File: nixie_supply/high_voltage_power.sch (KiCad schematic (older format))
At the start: 14 parts

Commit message: minor cleanups
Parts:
- C3: renamed from C?; value C_HV -> 10uF 315V
- D1: renamed from D?; value D_HV -> D_HV 400V
- gave numbers to parts that had none: 12
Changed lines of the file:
@@
 $EndDescr
 $Comp
-L 4047 U?
+L 4047 U2
 U 1 1 590CECA6
 P 4200 3000
-F 0 "U?" H 4200 2950 60  0000 C CNN
+F 0 "U2" H 4200 2950 60  0000 C CNN
 F 1 "4047" H 4200 2850 60  0000 C CNN
 F 2 "" H 4200 2950 60  0001 C CNN
@@
 $EndComp
 $Comp
-L GND #PWR?
+L GND #PWR03
 U 1 1 590CED04
 P 3200 3750
-F 0 "#PWR?" H 3200 3500 50  0001 C CNN
+F 0 "#PWR03" H 3200 3500 50  0001 C CNN
 F 1 "GND" H 3200 3600 50  0000 C CNN
 F 2 "" H 3200 3750 50  0000 C CNN
@@
 $EndComp
 $Comp
-L C C?
+L C C1
 U 1 1 590CF22D
 P 2950 2800
-F 0 "C?" H 2975 2900 50  0000 L CNN
+F 0 "C1" H 2975 2900 50  0000 L CNN
 F 1 "0.001uF" H 2650 2700 50  0000 L CNN
 F 2 "" H 2988 2650 50  0000 C CNN
@@
 $EndComp
 $Comp
-L R R?
+L R R4
 U 1 1 590CF24E
 P 3200 2800
-F 0 "R?" V 3280 2800 50  0000 C CNN
+F 0 "R4" V 3280 2800 50  0000 C CNN
 F 1 "10K" V 3200 2800 50  0000 C CNN
 F 2 "" V 3130 2800 50  0000 C CNN
@@
 $EndComp
 $Comp
-L GND #PWR?
+L GND #PWR04
 U 1 1 590CF44C
 P 5100 3400
-F 0 "#PWR?" H 5100 3150 50  0001 C CNN
+F 0 "#PWR04" H 5100 3150 50  0001 C CNN
 F 1 "GND" H 5100 3250 50  0000 C CNN
 F 2 "" H 5100 3400 50  0000 C CNN
@@
 NoConn ~ 4900 3050
 $Comp
-L R R?
+L R R6
 U 1 1 590CF674
 P 5400 3150
-F 0 "R?" V 5480 3150 50  0000 C CNN
+F 0 "R6" V 5480 3150 50  0000 C CNN
 F 1 "120" V 5400 3150 50  0000 C CNN
 F 2 "" V 5330 3150 50  0000 C CNN
@@
 	4900 3150 5250 3150
 $Comp
-L FQPF4N90CT Q?
+L FQPF4N90CT Q1
 U 1 1 590CFA7D
 P 5950 3100
-F 0 "Q?" H 6150 3175 50  0000 L CNN
+F 0 "Q1" H 6150 3175 50  0000 L CNN
 F 1 "FQPF4N90CT" H 6150 3100 50  0000 L CNN
 F 2 "TO_220" H 6150 3025 50  0001 L CIN
@@
 	5550 3150 5750 3150
 $Comp
-L L L?
+L L L1
 U 1 1 590CFB8C
 P 6050 2650
-F 0 "L?" V 6000 2650 50  0000 C CNN
+F 0 "L1" V 6000 2650 50  0000 C CNN
 F 1 "100uH" V 6125 2650 50  0000 C CNN
 F 2 "" H 6050 2650 50  0000 C CNN
@@
 	6050 2450 6050 2500
 $Comp
-L GND #PWR?
+L GND #PWR05
 U 1 1 590CFDA8
 P 6050 3400
-F 0 "#PWR?" H 6050 3150 50  0001 C CNN
+F 0 "#PWR05" H 6050 3150 50  0001 C CNN
 F 1 "GND" H 6050 3250 50  0000 C CNN
 F 2 "" H 6050 3400 50  0000 C CNN
@@
 	6050 3300 6050 3400
 $Comp
-L D_HV D?
+L D_HV D1
 U 1 1 590CFF0A
 P 6500 2850
-F 0 "D?" H 6500 2950 50  0000 C CNN
-F 1 "D_HV" H 6500 2750 50  0000 C CNN
+F 0 "D1" H 6500 2950 50  0000 C CNN
+F 1 "D_HV 400V" H 6500 2750 50  0000 C CNN
 F 2 "" H 6500 2850 50  0000 C CNN
 F 3 "" H 6500 2850 50  0000 C CNN
@@
 Connection ~ 6050 2850
 $Comp
-L C_HV C?
+L C_HV C3
 U 1 1 590D050D
 P 6950 3100
-F 0 "C?" H 6975 3200 50  0000 L CNN
-F 1 "C_HV" H 6975 3000 50  0000 L CNN
+F 0 "C3" H 6975 3200 50  0000 L CNN
+F 1 "10uF 315V" H 6975 3000 50  0000 L CNN
 F 2 "" H 6988 2950 50  0000 C CNN
 F 3 "" H 6950 3100 50  0000 C CNN
@@
 $EndComp
 Wire Wire Line
-	6650 2850 6950 2850
+	6650 2850 7200 2850
 Wire Wire Line
 	6950 2650 6950 2950
 $Comp
-L GND #PWR?
+L GND #PWR06
 U 1 1 590D056B
 P 6950 3400
-F 0 "#PWR?" H 6950 3150 50  0001 C CNN
+F 0 "#PWR06" H 6950 3150 50  0001 C CNN
 F 1 "GND" H 6950 3250 50  0000 C CNN
 F 2 "" H 6950 3400 50  0000 C CNN
@@
 Connection ~ 6950 2850
 $Comp
-L LM741 U?
+L LM741 U1
 U 1 1 590D1633
 P 3700 4700
-F 0 "U?" H 3700 4950 50  0000 L CNN
+F 0 "U1" H 3700 4950 50  0000 L CNN
 F 1 "LM741" H 3700 4850 50  0000 L CNN
 F 2 "" H 3750 4750 50  0000 C CNN
@@
 	4900 4700 4900 3250
 $Comp
-L GND #PWR?
+L GND #PWR07
 U 1 1 590D19B4
 P 3600 5100
-F 0 "#PWR?" H 3600 4850 50  0001 C CNN
+F 0 "#PWR07" H 3600 4850 50  0001 C CNN
 F 1 "GND" H 3600 4950 50  0000 C CNN
 F 2 "" H 3600 5100 50  0000 C CNN
@@
 	3600 5000 3600 5100
 $Comp
-L +5V #PWR?
+L +5V #PWR08
 U 1 1 590D1D3C
 P 2600 4800
-F 0 "#PWR?" H 2600 4650 50  0001 C CNN
+F 0 "#PWR08" H 2600 4650 50  0001 C CNN
 F 1 "+5V" H 2600 4940 50  0000 C CNN
 F 2 "" H 2600 4800 50  0000 C CNN
@@
 $EndComp
 $Comp
-L R R?
+L R R1
 U 1 1 590D1D88
 P 2850 4600
-F 0 "R?" V 2930 4600 50  0000 C CNN
+F 0 "R1" V 2930 4600 50  0000 C CNN
 F 1 "220K" V 2850 4600 50  0000 C CNN
 F 2 "" V 2780 4600 50  0000 C CNN
@@
 $EndComp
 $Comp
-L R R?
+L R R3
 U 1 1 590D1DB1
 P 3050 5150
-F 0 "R?" V 3130 5150 50  0000 C CNN
+F 0 "R3" V 3130 5150 50  0000 C CNN
 F 1 "4.7K" V 3050 5150 50  0000 C CNN
 F 2 "" V 2980 5150 50  0000 C CNN
@@
 $EndComp
 $Comp
-L R R?
+L R R2
 U 1 1 590D1DDC
 P 2850 4800
-F 0 "R?" V 2930 4800 50  0000 C CNN
+F 0 "R2" V 2930 4800 50  0000 C CNN
 F 1 "1.2K" V 2850 4800 50  0000 C CNN
 F 2 "" V 2780 4800 50  0000 C CNN
@@
 $EndComp
 $Comp
-L R R?
+L R R5
 U 1 1 590D1E09
 P 3250 5150
-F 0 "R?" V 3330 5150 50  0000 C CNN
+F 0 "R5" V 3330 5150 50  0000 C CNN
 F 1 "4.7K" V 3250 5150 50  0000 C CNN
 F 2 "" V 3180 5150 50  0000 C CNN
@@
 Connection ~ 3250 4800
 $Comp
-L GND #PWR?
+L GND #PWR09
 U 1 1 590D2323
 P 3150 5400
-F 0 "#PWR?" H 3150 5150 50  0001 C CNN
+F 0 "#PWR09" H 3150 5150 50  0001 C CNN
 F 1 "GND" H 3150 5250 50  0000 C CNN
 F 2 "" H 3150 5400 50  0000 C CNN
@@
 220V
 $Comp
-L +5V #PWR?
+L +5V #PWR010
 U 1 1 590D45F5
 P 6050 3900
-F 0 "#PWR?" H 6050 3750 50  0001 C CNN
+F 0 "#PWR010" H 6050 3750 50  0001 C CNN
 F 1 "+5V" H 6050 4040 50  0000 C CNN
 F 2 "" H 6050 3900 50  0000 C CNN
@@
 GND
 $Comp
-L GND #PWR?
+L GND #PWR011
 U 1 1 590D826E
 P 6200 4550
-F 0 "#PWR?" H 6200 4300 50  0001 C CNN
+F 0 "#PWR011" H 6200 4300 50  0001 C CNN
 F 1 "GND" H 6200 4400 50  0000 C CNN
 F 2 "" H 6200 4550 50  0000 C CNN
@@
 	6000 4550 6200 4550
 $Comp
-L +12V #PWR?
+L +12V #PWR012
 U 1 1 5910BACF
 P 3200 3300
-F 0 "#PWR?" H 3200 3150 50  0001 C CNN
+F 0 "#PWR012" H 3200 3150 50  0001 C CNN
 F 1 "+12V" H 3200 3440 50  0000 C CNN
 F 2 "" H 3200 3300 50  0000 C CNN
@@
 $EndComp
 $Comp
-L +12V #PWR?
+L +12V #PWR013
 U 1 1 5910BAFD
 P 5300 2550
-F 0 "#PWR?" H 5300 2400 50  0001 C CNN
+F 0 "#PWR013" H 5300 2400 50  0001 C CNN
 F 1 "+12V" H 5300 2690 50  0000 C CNN
 F 2 "" H 5300 2550 50  0000 C CNN
@@
 $EndComp
 $Comp
-L +12V #PWR?
+L +12V #PWR014
 U 1 1 5910BB2B
 P 6050 2450
-F 0 "#PWR?" H 6050 2300 50  0001 C CNN
+F 0 "#PWR014" H 6050 2300 50  0001 C CNN
 F 1 "+12V" H 6050 2590 50  0000 C CNN
 F 2 "" H 6050 2450 50  0000 C CNN
@@
 $EndComp
 $Comp
-L +12V #PWR?
+L +12V #PWR015
 U 1 1 5910BB59
 P 6200 4350
-F 0 "#PWR?" H 6200 4200 50  0001 C CNN
+F 0 "#PWR015" H 6200 4200 50  0001 C CNN
 F 1 "+12V" H 6200 4490 50  0000 C CNN
 F 2 "" H 6200 4350 50  0000 C CNN
@@
 12V
 $Comp
-L +5V #PWR?
+L +5V #PWR016
 U 1 1 5910BD01
 P 3600 4300
-F 0 "#PWR?" H 3600 4150 50  0001 C CNN
+F 0 "#PWR016" H 3600 4150 50  0001 C CNN
 F 1 "+5V" H 3600 4440 50  0000 C CNN
 F 2 "" H 3600 4300 50  0000 C CNN
@@
 $EndComp
 $Comp
-L C C?
+L C C2
 U 1 1 5910C445
 P 3200 3550
-F 0 "C?" H 3225 3650 50  0000 L CNN
+F 0 "C2" H 3225 3650 50  0000 L CNN
 F 1 "0.1uF" H 3225 3450 50  0000 L CNN
 F 2 "" H 3238 3400 50  0000 C CNN
@@
 	3450 3750 3200 3750
 $Comp
-L +220V #PWR?
+L +220V #PWR017
 U 1 1 5910CAB3
 P 2600 4600
-F 0 "#PWR?" H 2600 4450 50  0001 C CNN
+F 0 "#PWR017" H 2600 4450 50  0001 C CNN
 F 1 "+220V" H 2600 4740 50  0000 C CNN
 F 2 "" H 2600 4600 50  0000 C CNN
@@
 $EndComp
 $Comp
-L +220V #PWR?
+L +220V #PWR018
 U 1 1 5910CAE3
 P 6950 2650
-F 0 "#PWR?" H 6950 2500 50  0001 C CNN
+F 0 "#PWR018" H 6950 2500 50  0001 C CNN
 F 1 "+220V" H 6950 2790 50  0000 C CNN
 F 2 "" H 6950 2650 50  0000 C CNN
@@
 $EndComp
 $Comp
-L +220V #PWR?
+L +220V #PWR019
 U 1 1 5910CB13
 P 6550 3900
-F 0 "#PWR?" H 6550 3750 50  0001 C CNN
+F 0 "#PWR019" H 6550 3750 50  0001 C CNN
 F 1 "+220V" H 6550 4040 50  0000 C CNN
 F 2 "" H 6550 3900 50  0000 C CNN
@@
 	1    0    0    -1
 $EndComp
+$Comp
+L PWR_FLAG #FLG020
+U 1 1 591378F6
+P 7200 2850
+F 0 "#FLG020" H 7200 2945 50  0001 C CNN
+F 1 "PWR_FLAG" H 7200 3030 50  0000 C CNN
+F 2 "" H 7200 2850 50  0000 C CNN
+F 3 "" H 7200 2850 50  0000 C CNN
+	1    7200 2850
+	1    0    0    -1
+$EndComp

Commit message: Footprint associations
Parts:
- C1: footprint (none) -> Capacitors_THT:C_Disc_D5.0mm_W2.5mm_P5.00mm
- C2: footprint (none) -> Capacitors_THT:C_Axial_L5.1mm_D3.1mm_P7.50mm_Horizontal
- C3: footprint (none) -> Capacitors_THT:CP_Radial_D10.0mm_P3.80mm
- D1: footprint (none) -> Diodes_THT:D_T-1_P5.08mm_Horizontal
- L1: footprint (none) -> Inductors_NEOSID:Neosid_Inductor_Sd8
- Q1: footprint TO_220 -> TO_SOT_Packages_THT:TO-220_Vertical
- R1, R3: footprint (none) -> hv:R_Axial_DIN0309_L9.0mm_D3.2mm_P12.70mm_Horizontal_Thick
- R2, R4, R5, R6: footprint (none) -> Resistors_THT:R_Axial_DIN0207_L6.3mm_D2.5mm_P10.16mm_Horizontal
- U1: footprint (none) -> Housings_DIP:DIP-8_W7.62mm
- U2: footprint (none) -> Housings_DIP:DIP-14_W7.62mm
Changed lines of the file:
@@
 F 0 "U2" H 4200 2950 60  0000 C CNN
 F 1 "4047" H 4200 2850 60  0000 C CNN
-F 2 "" H 4200 2950 60  0001 C CNN
+F 2 "Housings_DIP:DIP-14_W7.62mm" H 4200 2950 60  0001 C CNN
 F 3 "" H 4200 2950 60  0001 C CNN
 	1    4200 3000
@@
 F 0 "C1" H 2975 2900 50  0000 L CNN
 F 1 "0.001uF" H 2650 2700 50  0000 L CNN
-F 2 "" H 2988 2650 50  0000 C CNN
+F 2 "Capacitors_THT:C_Disc_D5.0mm_W2.5mm_P5.00mm" H 2988 2650 50  0001 C CNN
 F 3 "" H 2950 2800 50  0000 C CNN
 	1    2950 2800
@@
 F 0 "R4" V 3280 2800 50  0000 C CNN
 F 1 "10K" V 3200 2800 50  0000 C CNN
-F 2 "" V 3130 2800 50  0000 C CNN
+F 2 "Resistors_THT:R_Axial_DIN0207_L6.3mm_D2.5mm_P10.16mm_Horizontal" V 3130 2800 50  0001 C CNN
 F 3 "" H 3200 2800 50  0000 C CNN
 	1    3200 2800
@@
 F 0 "R6" V 5480 3150 50  0000 C CNN
 F 1 "120" V 5400 3150 50  0000 C CNN
-F 2 "" V 5330 3150 50  0000 C CNN
+F 2 "Resistors_THT:R_Axial_DIN0207_L6.3mm_D2.5mm_P10.16mm_Horizontal" V 5330 3150 50  0001 C CNN
 F 3 "" H 5400 3150 50  0000 C CNN
 	1    5400 3150
@@
 U 1 1 590CFA7D
 P 5950 3100
+AR Path="/590CFA7D" Ref="Q1"  Part="1"
+AR Path="/5910AEC0/590CFA7D" Ref="Q1"  Part="1"
 F 0 "Q1" H 6150 3175 50  0000 L CNN
 F 1 "FQPF4N90CT" H 6150 3100 50  0000 L CNN
-F 2 "TO_220" H 6150 3025 50  0001 L CIN
+F 2 "TO_SOT_Packages_THT:TO-220_Vertical" H 6150 3025 50  0001 L CIN
 F 3 "" H 5950 3100 50  0000 L CNN
 	1    5950 3100
 	1    0    0    -1
 $EndComp
-Wire Wire Line
-	5550 3150 5750 3150
 $Comp
 L L L1
@@
 F 0 "L1" V 6000 2650 50  0000 C CNN
 F 1 "100uH" V 6125 2650 50  0000 C CNN
-F 2 "" H 6050 2650 50  0000 C CNN
+F 2 "Inductors_NEOSID:Neosid_Inductor_Sd8" H 6050 2650 50  0001 C CNN
 F 3 "" H 6050 2650 50  0000 C CNN
 	1    6050 2650
 	1    0    0    -1
 $EndComp
-Wire Wire Line
-	6050 2800 6050 2900
 Wire Wire Line
 	6050 2450 6050 2500
@@
 	1    0    0    -1
 $EndComp
-Wire Wire Line
-	6050 3300 6050 3400
 $Comp
 L D_HV D1
@@
 F 0 "D1" H 6500 2950 50  0000 C CNN
 F 1 "D_HV 400V" H 6500 2750 50  0000 C CNN
-F 2 "" H 6500 2850 50  0000 C CNN
+F 2 "Diodes_THT:D_T-1_P5.08mm_Horizontal" H 6500 2850 50  0001 C CNN
 F 3 "" H 6500 2850 50  0000 C CNN
 	1    6500 2850
@@
 F 0 "C3" H 6975 3200 50  0000 L CNN
 F 1 "10uF 315V" H 6975 3000 50  0000 L CNN
-F 2 "" H 6988 2950 50  0000 C CNN
+F 2 "Capacitors_THT:CP_Radial_D10.0mm_P3.80mm" H 6988 2950 50  0001 C CNN
 F 3 "" H 6950 3100 50  0000 C CNN
 	1    6950 3100
@@
 F 0 "U1" H 3700 4950 50  0000 L CNN
 F 1 "LM741" H 3700 4850 50  0000 L CNN
-F 2 "" H 3750 4750 50  0000 C CNN
+F 2 "Housings_DIP:DIP-8_W7.62mm" H 3750 4750 50  0001 C CNN
 F 3 "" H 3850 4850 50  0000 C CNN
 	1    3700 4700
@@
 F 0 "R1" V 2930 4600 50  0000 C CNN
 F 1 "220K" V 2850 4600 50  0000 C CNN
-F 2 "" V 2780 4600 50  0000 C CNN
+F 2 "hv:R_Axial_DIN0309_L9.0mm_D3.2mm_P12.70mm_Horizontal_Thick" V 2780 4600 50  0001 C CNN
 F 3 "" H 2850 4600 50  0000 C CNN
 	1    2850 4600
@@
 F 0 "R3" V 3130 5150 50  0000 C CNN
 F 1 "4.7K" V 3050 5150 50  0000 C CNN
-F 2 "" V 2980 5150 50  0000 C CNN
+F 2 "hv:R_Axial_DIN0309_L9.0mm_D3.2mm_P12.70mm_Horizontal_Thick" V 2980 5150 50  0001 C CNN
 F 3 "" H 3050 5150 50  0000 C CNN
 	1    3050 5150
@@
 F 0 "R2" V 2930 4800 50  0000 C CNN
 F 1 "1.2K" V 2850 4800 50  0000 C CNN
-F 2 "" V 2780 4800 50  0000 C CNN
+F 2 "Resistors_THT:R_Axial_DIN0207_L6.3mm_D2.5mm_P10.16mm_Horizontal" V 2780 4800 50  0001 C CNN
 F 3 "" H 2850 4800 50  0000 C CNN
 	1    2850 4800
@@
 F 0 "R5" V 3330 5150 50  0000 C CNN
 F 1 "4.7K" V 3250 5150 50  0000 C CNN
-F 2 "" V 3180 5150 50  0000 C CNN
+F 2 "Resistors_THT:R_Axial_DIN0207_L6.3mm_D2.5mm_P10.16mm_Horizontal" V 3180 5150 50  0001 C CNN
 F 3 "" H 3250 5150 50  0000 C CNN
 	1    3250 5150
@@
 F 0 "C2" H 3225 3650 50  0000 L CNN
 F 1 "0.1uF" H 3225 3450 50  0000 L CNN
-F 2 "" H 3238 3400 50  0000 C CNN
+F 2 "Capacitors_THT:C_Axial_L5.1mm_D3.1mm_P7.50mm_Horizontal" H 3238 3400 50  0001 C CNN
 F 3 "" H 3200 3550 50  0000 C CNN
 	1    3200 3550
@@
 	1    0    0    -1
 $EndComp
+Wire Wire Line
+	6050 2800 6050 2900
+Wire Wire Line
+	6050 3300 6050 3400
+Wire Wire Line
+	5550 3150 5750 3150
 $EndSCHEMATC

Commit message: Clock board layout
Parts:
- U1: symbol LM741 -> LM741-RESCUE-nixie_supply
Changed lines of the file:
@@
 EESchema Schematic File Version 2
+LIBS:nixie_supply-rescue
 LIBS:power
 LIBS:device
@@
 Connection ~ 6950 2850
 $Comp
-L LM741 U1
+L LM741-RESCUE-nixie_supply U1
 U 1 1 590D1633
 P 3700 4700

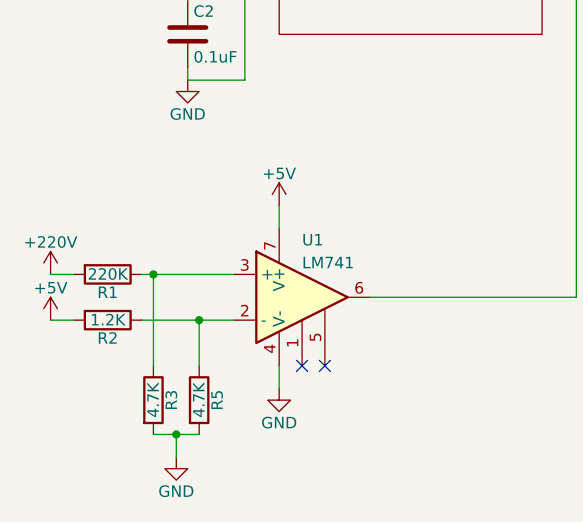
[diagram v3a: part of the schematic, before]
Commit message: Supply board mk2: reduced time base noise, upped some clearances, added ground plane
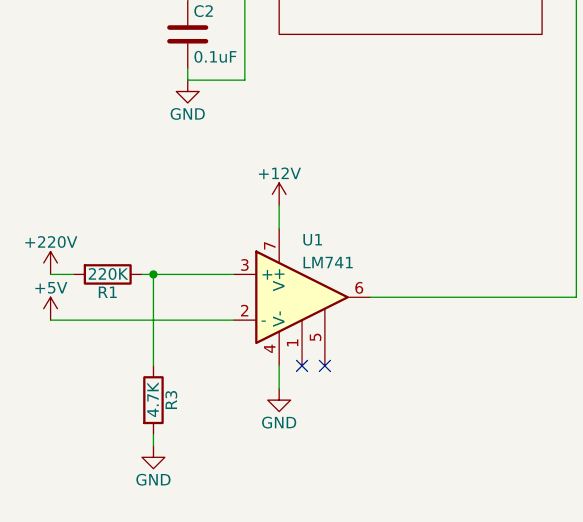
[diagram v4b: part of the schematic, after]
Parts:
- removed R2: 1.2K, Resistors_THT:R_Axial_DIN0207_L6.3mm_D2.5mm_P10.16mm_Horizontal, symbol R
- removed R5: 4.7K, Resistors_THT:R_Axial_DIN0207_L6.3mm_D2.5mm_P10.16mm_Horizontal, symbol R
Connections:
- net +12V: now also U1.7 (V+)
- net +5V: now also U1.2 (-); no longer U1.7 (V+)
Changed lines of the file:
@@
 $EndComp
-Wire Wire Line
-	3600 4300 3600 4400
 Wire Wire Line
 	3600 5000 3600 5100
@@
 	1    0    0    -1
 $EndComp
-$Comp
-L R R2
-U 1 1 590D1DDC
-P 2850 4800
-F 0 "R2" V 2930 4800 50  0000 C CNN
-F 1 "1.2K" V 2850 4800 50  0000 C CNN
-F 2 "Resistors_THT:R_Axial_DIN0207_L6.3mm_D2.5mm_P10.16mm_Horizontal" V 2780 4800 50  0001 C CNN
-F 3 "" H 2850 4800 50  0000 C CNN
-	1    2850 4800
-	0    1    1    0
-$EndComp
-$Comp
-L R R5
-U 1 1 590D1E09
-P 3250 5150
-F 0 "R5" V 3330 5150 50  0000 C CNN
-F 1 "4.7K" V 3250 5150 50  0000 C CNN
-F 2 "Resistors_THT:R_Axial_DIN0207_L6.3mm_D2.5mm_P10.16mm_Horizontal" V 3180 5150 50  0001 C CNN
-F 3 "" H 3250 5150 50  0000 C CNN
-	1    3250 5150
-	1    0    0    -1
-$EndComp
 Wire Wire Line
 	2600 4600 2700 4600
 Wire Wire Line
 	3000 4600 3400 4600
-Wire Wire Line
-	3400 4800 3000 4800
-Wire Wire Line
-	2600 4800 2700 4800
 Wire Wire Line
 	3050 5000 3050 4600
 Connection ~ 3050 4600
-Wire Wire Line
-	3250 5000 3250 4800
-Connection ~ 3250 4800
 $Comp
 L GND #PWR09
 U 1 1 590D2323
-P 3150 5400
-F 0 "#PWR09" H 3150 5150 50  0001 C CNN
-F 1 "GND" H 3150 5250 50  0000 C CNN
-F 2 "" H 3150 5400 50  0000 C CNN
-F 3 "" H 3150 5400 50  0000 C CNN
-	1    3150 5400
-	1    0    0    -1
-$EndComp
-Wire Wire Line
-	3050 5300 3250 5300
-Wire Wire Line
-	3150 5300 3150 5400
-Connection ~ 3150 5300
+P 3050 5350
+F 0 "#PWR09" H 3050 5100 50  0001 C CNN
+F 1 "GND" H 3050 5200 50  0000 C CNN
+F 2 "" H 3050 5350 50  0000 C CNN
+F 3 "" H 3050 5350 50  0000 C CNN
+	1    3050 5350
+	1    0    0    -1
+$EndComp
 NoConn ~ 3700 5000
 NoConn ~ 3800 5000
@@
 12V
 $Comp
-L +5V #PWR016
-U 1 1 5910BD01
-P 3600 4300
-F 0 "#PWR016" H 3600 4150 50  0001 C CNN
-F 1 "+5V" H 3600 4440 50  0000 C CNN
-F 2 "" H 3600 4300 50  0000 C CNN
-F 3 "" H 3600 4300 50  0000 C CNN
-	1    3600 4300
-	1    0    0    -1
-$EndComp
-$Comp
 L C C2
 U 1 1 5910C445
@@
 Wire Wire Line
 	5550 3150 5750 3150
+Wire Wire Line
+	3050 5300 3050 5350
+Wire Wire Line
+	2600 4800 3400 4800
+$Comp
+L +12V #PWR?
+U 1 1 5985A445
+P 3600 4300
+F 0 "#PWR?" H 3600 4150 50  0001 C CNN
+F 1 "+12V" H 3600 4440 50  0000 C CNN
+F 2 "" H 3600 4300 50  0001 C CNN
+F 3 "" H 3600 4300 50  0001 C CNN
+	1    3600 4300
+	1    0    0    -1
+$EndComp
+Wire Wire Line
+	3600 4400 3600 4300
 $EndSCHEMATC

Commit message: Added more noise reduction to clock signal, added top ground plane
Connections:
- net +220V renamed +240V
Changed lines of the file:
@@
 Wire Wire Line
 	6650 2850 7200 2850
-Wire Wire Line
-	6950 2650 6950 2950
 $Comp
 L GND #PWR06
@@
 $EndComp
 Wire Wire Line
-	2600 4600 2700 4600
-Wire Wire Line
 	3000 4600 3400 4600
 Wire Wire Line
@@
 Text HLabel 6000 4000 0    60   Input ~ 0
 5V
-Text HLabel 6450 4000 0    60   Input ~ 0
-220V
 $Comp
 L +5V #PWR010
@@
 	6050 4000 6000 4000
 Wire Wire Line
-	6550 3900 6550 4000
-Wire Wire Line
-	6550 4000 6450 4000
-Wire Wire Line
 	6200 4350 6000 4350
 Wire Wire Line
@@
 	3450 3750 3200 3750
 $Comp
-L +220V #PWR017
-U 1 1 5910CAB3
-P 2600 4600
-F 0 "#PWR017" H 2600 4450 50  0001 C CNN
-F 1 "+220V" H 2600 4740 50  0000 C CNN
-F 2 "" H 2600 4600 50  0000 C CNN
-F 3 "" H 2600 4600 50  0000 C CNN
-	1    2600 4600
-	1    0    0    -1
-$EndComp
-$Comp
-L +220V #PWR018
-U 1 1 5910CAE3
-P 6950 2650
-F 0 "#PWR018" H 6950 2500 50  0001 C CNN
-F 1 "+220V" H 6950 2790 50  0000 C CNN
-F 2 "" H 6950 2650 50  0000 C CNN
-F 3 "" H 6950 2650 50  0000 C CNN
-	1    6950 2650
-	1    0    0    -1
-$EndComp
-$Comp
-L +220V #PWR019
-U 1 1 5910CB13
-P 6550 3900
-F 0 "#PWR019" H 6550 3750 50  0001 C CNN
-F 1 "+220V" H 6550 4040 50  0000 C CNN
-F 2 "" H 6550 3900 50  0000 C CNN
-F 3 "" H 6550 3900 50  0000 C CNN
-	1    6550 3900
-	1    0    0    -1
-$EndComp
-$Comp
-L PWR_FLAG #FLG020
+L PWR_FLAG #FLG017
 U 1 1 591378F6
 P 7200 2850
-F 0 "#FLG020" H 7200 2945 50  0001 C CNN
+F 0 "#FLG017" H 7200 2945 50  0001 C CNN
 F 1 "PWR_FLAG" H 7200 3030 50  0000 C CNN
 F 2 "" H 7200 2850 50  0000 C CNN
@@
 	2600 4800 3400 4800
 $Comp
-L +12V #PWR?
+L +12V #PWR018
 U 1 1 5985A445
 P 3600 4300
-F 0 "#PWR?" H 3600 4150 50  0001 C CNN
+F 0 "#PWR018" H 3600 4150 50  0001 C CNN
 F 1 "+12V" H 3600 4440 50  0000 C CNN
 F 2 "" H 3600 4300 50  0001 C CNN
@@
 Wire Wire Line
 	3600 4400 3600 4300
+$Comp
+L +240V #PWR019
+U 1 1 598766BE
+P 6550 3900
+F 0 "#PWR019" H 6550 3750 50  0001 C CNN
+F 1 "+240V" H 6550 4040 50  0000 C CNN
+F 2 "" H 6550 3900 50  0000 C CNN
+F 3 "" H 6550 3900 50  0000 C CNN
+	1    6550 3900
+	1    0    0    -1
+$EndComp
+Text HLabel 6500 4000 0    60   Input ~ 0
+240V
+Wire Wire Line
+	6500 4000 6550 4000
+Wire Wire Line
+	6550 4000 6550 3900
+$Comp
+L +240V #PWR020
+U 1 1 59876987
+P 6950 2600
+F 0 "#PWR020" H 6950 2450 50  0001 C CNN
+F 1 "+240V" H 6950 2740 50  0000 C CNN
+F 2 "" H 6950 2600 50  0000 C CNN
+F 3 "" H 6950 2600 50  0000 C CNN
+	1    6950 2600
+	1    0    0    -1
+$EndComp
+Wire Wire Line
+	6950 2600 6950 2950
+$Comp
+L +240V #PWR?
+U 1 1 59877765
+P 2600 4600
+F 0 "#PWR?" H 2600 4450 50  0001 C CNN
+F 1 "+240V" H 2600 4740 50  0000 C CNN
+F 2 "" H 2600 4600 50  0000 C CNN
+F 3 "" H 2600 4600 50  0000 C CNN
+	1    2600 4600
+	1    0    0    -1
+$EndComp
+Wire Wire Line
+	2600 4600 2700 4600
 $EndSCHEMATC
